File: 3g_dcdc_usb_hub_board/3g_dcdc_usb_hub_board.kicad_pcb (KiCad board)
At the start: 2 copper layers, 17 x 36.8 mm, 31 parts, among them J1 G2116, J2 Conn_01x04, U1 DC_DC_BREAKOUT, U2 GL850G, Y1 Crystal

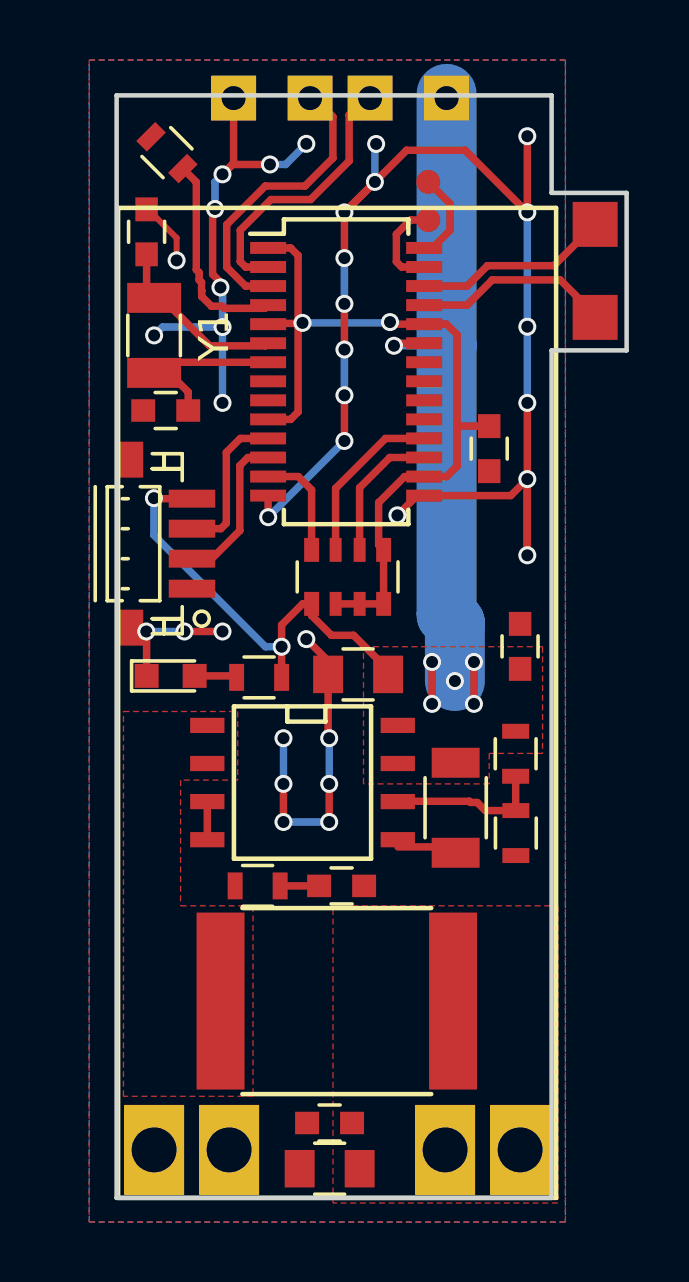
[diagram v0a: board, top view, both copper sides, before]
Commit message: Finished the GL850G-based USB hub&DCDC board
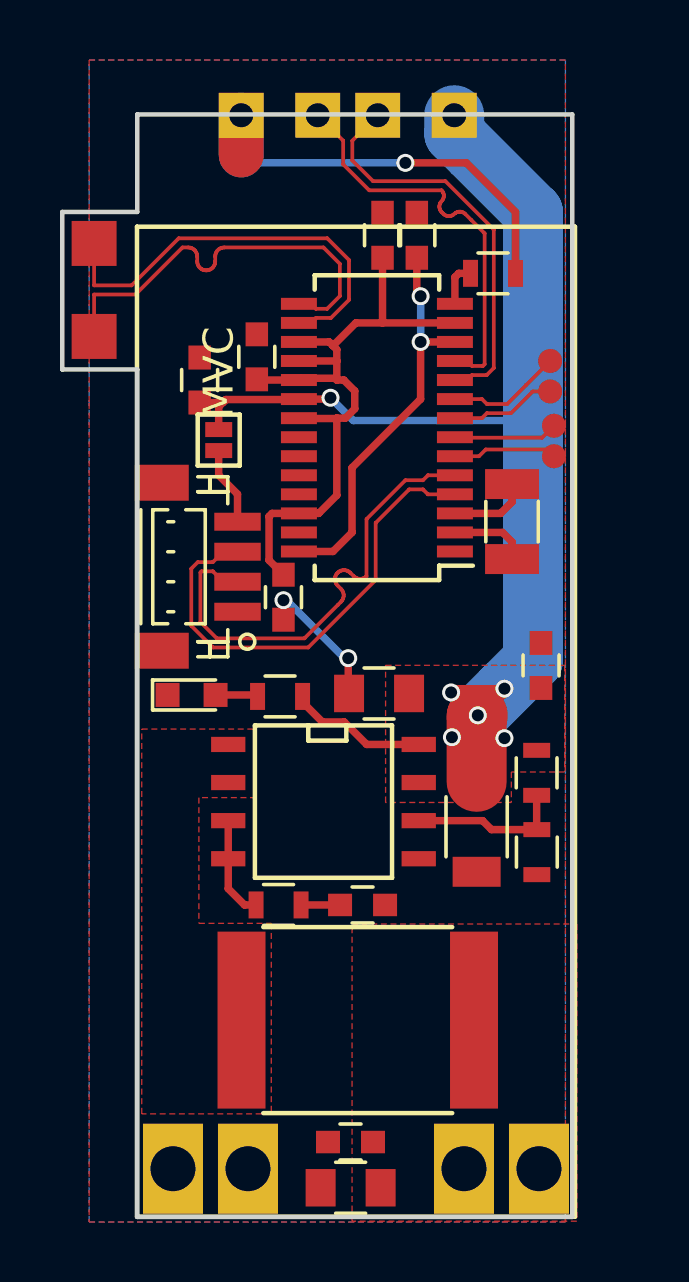
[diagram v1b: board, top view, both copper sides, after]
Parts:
- removed C7: C_Small, Capacitors_SMD:C_0603
- removed RN1: R_Pack04, Resistors_SMD:R_Array_Convex_4x0603
- added C10: C, Capacitors_SMD:C_0603, F.Cu at (146.8, 101.7)
- added C11: C, Capacitors_SMD:C_0603, F.Cu at (151.3, 89.7)
- added C12: C, Capacitors_SMD:C_0603, F.Cu at (144.0, 94.5)
- added JP1: MVC, footprints:GS2_SMALL, F.Cu at (144.7, 96.8)
- added TP10: UB+, Measurement_Points:Measurement_Point_Round-SMD-Pad_Small, F.Cu at (155.7, 93.9)
- added TP9: UB-, Measurement_Points:Measurement_Point_Round-SMD-Pad_Small, F.Cu at (155.7, 94.9)
- ?: moved to B.Cu
- C6: value C_Small -> C
- R4: value 680R -> 2K7
- U2: value GL850G -> FE1.1s
- moved ? 24.5 mm to (136.6, 127.8), turned to 0 degrees
- moved TP3 16.7 mm to (140.5, 93.0)
- moved TP4 16.7 mm to (140.5, 89.9)
- moved Y1 13.4 mm to (154.4, 99.2)
- moved R4 11.6 mm to (153.8, 90.9), turned to 0 degrees
- moved TP8 9.14 mm to (155.8, 96.0), turned to 0 degrees
- moved TP7 8.92 mm to (155.8, 97.0), turned to 0 degrees
- moved C8 7.95 mm to (150.1, 89.7), turned to 90 degrees
- moved C6 5.55 mm to (145.9, 93.7), turned to 270 degrees
- moved U2 2.13 mm to (149.9, 96.1), turned to 180 degrees
- moved J2 1.70 mm to (144.0, 100.7)
- moved C3 0.94 mm to (155.4, 104.0)
- moved R5 0.94 mm to (146.6, 112.0)
- moved C1 0.94 mm to (149.0, 119.9)
- moved C2 0.94 mm to (149.1, 121.4)
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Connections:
- C6 pad 1: Net-(C6-Pad1) -> GND
- C6 pad 2: GND -> +3V3
- J2 pad 4: +5V -> Net-(J2-Pad4)
- R4 pad 1: GND -> Net-(R4-Pad1)
- R4 pad 2: Net-(R4-Pad2) -> GND
- R5 pad 2: (no net) -> Net-(J1-Pad3)
- U2 pad 1: +3V3 -> GND
- U2 pad 10: +3V3 -> UE-
- U2 pad 11: UG- -> UE+
- U2 pad 12: UG+ -> +1V8
- U2 pad 13: Net-(RN1-Pad8) -> +3V3
- U2 pad 14: GND -> Net-(R4-Pad1)
- U2 pad 15: GND -> UIN-
- U2 pad 16: +3V3 -> UIN+
- U2 pad 17: Net-(RN1-Pad6) -> +3V3
- U2 pad 18: Net-(RN1-Pad7) -> +3V3
- U2 pad 19: (no net) -> +3V3
- U2 pad 2: UE- -> Net-(U2-Pad2)
- U2 pad 20: (no net) -> +5V
- U2 pad 21: (no net) -> +3V3
- U2 pad 23: +5V -> (no net)
- U2 pad 24: +3V3 -> (no net)
- U2 pad 25: UIN- -> (no net)
- U2 pad 26: UIN+ -> +3V3
- U2 pad 27: UA- -> (no net)
- U2 pad 28: UA+ -> +1V8
- U2 pad 3: UE+ -> Net-(U2-Pad3)
- U2 pad 4: Net-(R4-Pad2) -> UG-
- U2 pad 5: +3V3 -> UG+
- U2 pad 6: Net-(C6-Pad1) -> UA-
- U2 pad 7: Net-(C7-Pad2) -> UA+
- U2 pad 8: (no net) -> UB-
- U2 pad 9: (no net) -> UB+
- Y1 pad 1: Net-(C7-Pad2) -> Net-(U2-Pad2)
- Y1 pad 2: Net-(C6-Pad1) -> Net-(U2-Pad3)
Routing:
- net GND: track 79.0 -> 19.4 mm, vias 35 -> 3
- net +1V8: track 0.00 -> 13.3 mm, vias 0 -> 2
- net UG-: track 5.17 -> 16.1 mm
- net UG+: track 5.20 -> 16.1 mm
- net UIN+: track 6.55 -> 14.2 mm
- net UIN-: track 6.62 -> 14.2 mm
- net Net-(R4-Pad2): track 6.94 -> 0.00 mm
- net Net-(C6-Pad1): track 6.05 -> 0.00 mm
- net Net-(C7-Pad2): track 5.96 -> 0.00 mm
- net +5V: track 44.3 -> 50.0 mm, vias 8 -> 6
- net Net-(RN1-Pad7): track 5.69 -> 0.00 mm
- net Net-(RN1-Pad6): track 4.64 -> 0.00 mm
- net UE-: track 9.16 -> 13.6 mm
- net +3V3: track 27.5 -> 23.5 mm, vias 2 -> 0
- net UB+: track 0.00 -> 3.84 mm
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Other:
- outline, holes or cut-outs redrawn
- net class Default: clearance 0.2 -> 0.15
- rule trace_clearance: 0.2 -> 0.15
- rule trace_min: 0.2 -> 0.1
- board text added: "DC-DC&USB board (for use with 3G modems) based on FE1.1s by CRImier, v1.0"
- board text removed: "DC-DC&USB board (for use with 3G modems) by CRImier, v1.0"
